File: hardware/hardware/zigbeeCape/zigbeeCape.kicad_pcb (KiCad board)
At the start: 4 copper layers, 63.5 x 54.6 mm, 144 parts, among them J1 Conn_ARM_JTAG_SWD_10, SW1 SW_MEC_5E, SW2 SW_MEC_5E, SW3 SW_MEC_5E, SW4 SW_MEC_5E, SW5 SW_MEC_5E, U1 CC1352R, U2 0.8Ghz_and_2.4GHz_Filter, U3 SMA_Antenna, U4 BeagleBone_P8, U5 BeagleBone_P9, Y1 32.768kHz, Y2 48MHz

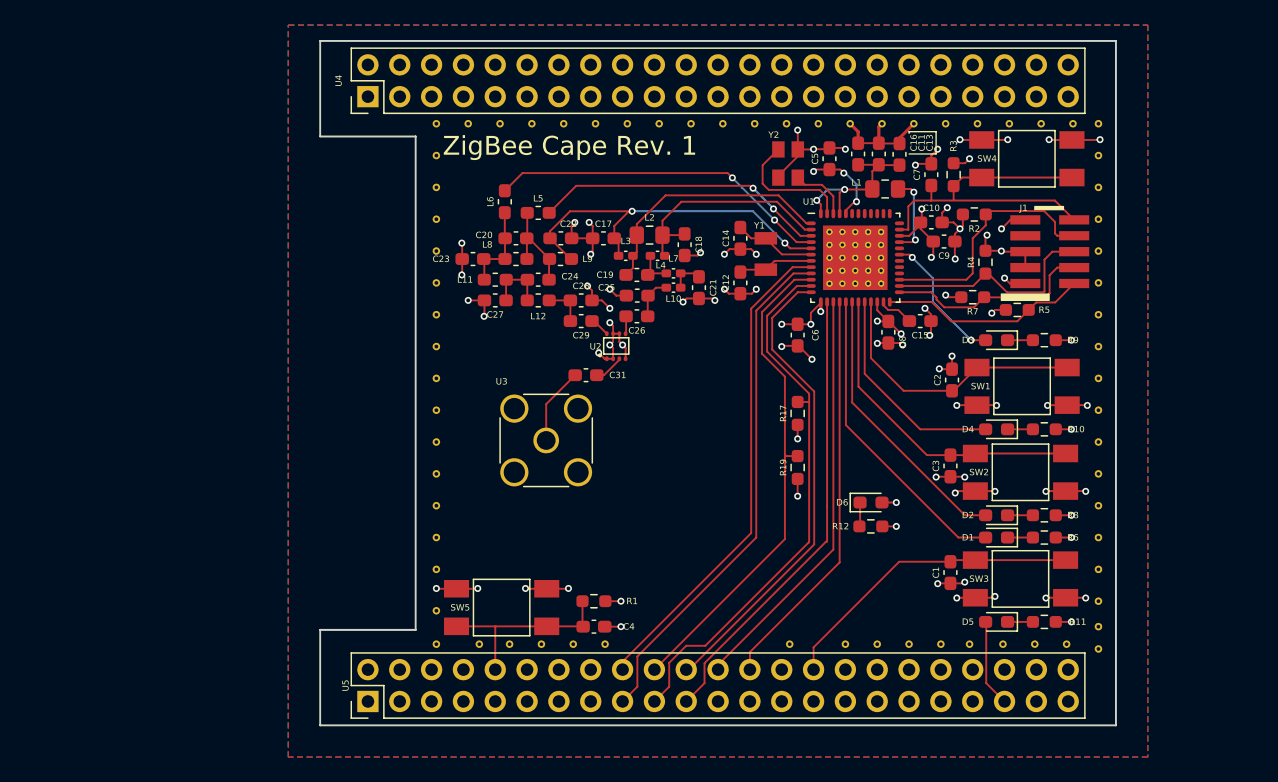
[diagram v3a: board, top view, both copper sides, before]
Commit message: Added more ground vias and silkscreen pin labels for the headers
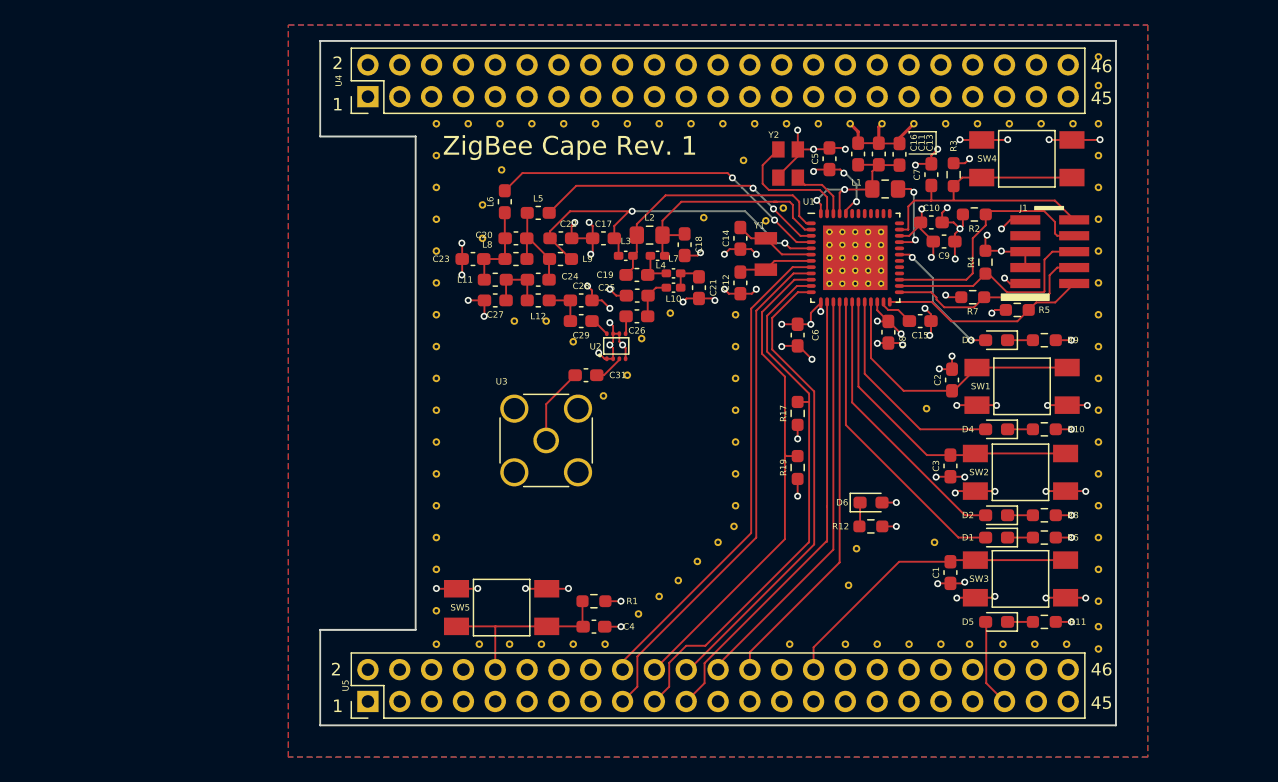
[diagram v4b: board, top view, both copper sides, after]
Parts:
- added REF**: ViaStitch-0.6mm, zigbeeCape:ViaStitch-0.6mm, F.Cu at (14.5, -44.3)
- added REF**: ViaStitch-0.6mm, zigbeeCape:ViaStitch-0.6mm, F.Cu at (25.7, -30.9)
- added REF**: ViaStitch-0.6mm, zigbeeCape:ViaStitch-0.6mm, F.Cu at (27.9, -32.9)
- added REF**: ViaStitch-0.6mm, zigbeeCape:ViaStitch-0.6mm, F.Cu at (25.4, -8.89)
- added REF**: ViaStitch-0.6mm, zigbeeCape:ViaStitch-0.6mm, F.Cu at (27.1, -10.3)
- added REF**: ViaStitch-0.6mm, zigbeeCape:ViaStitch-0.6mm, F.Cu at (28.6, -11.6)
- added REF**: ViaStitch-0.6mm, zigbeeCape:ViaStitch-0.6mm, F.Cu at (30.1, -13.1)
- added REF**: ViaStitch-0.6mm, zigbeeCape:ViaStitch-0.6mm, F.Cu at (31.8, -14.6)
- added REF**: ViaStitch-0.6mm, zigbeeCape:ViaStitch-0.6mm, F.Cu at (33.0, -15.9)
- added REF**: ViaStitch-0.6mm, zigbeeCape:ViaStitch-0.6mm, F.Cu at (33.1, -17.5)
- added REF**: ViaStitch-0.6mm, zigbeeCape:ViaStitch-0.6mm, F.Cu at (33.1, -20.1)
- added REF**: ViaStitch-0.6mm, zigbeeCape:ViaStitch-0.6mm, F.Cu at (13.0, -41.5)
- added REF**: ViaStitch-0.6mm, zigbeeCape:ViaStitch-0.6mm, F.Cu at (33.1, -22.6)
- added REF**: ViaStitch-0.6mm, zigbeeCape:ViaStitch-0.6mm, F.Cu at (33.1, -25.1)
- added REF**: ViaStitch-0.6mm, zigbeeCape:ViaStitch-0.6mm, F.Cu at (33.1, -27.7)
- added REF**: ViaStitch-0.6mm, zigbeeCape:ViaStitch-0.6mm, F.Cu at (33.1, -30.2)
- added REF**: ViaStitch-0.6mm, zigbeeCape:ViaStitch-0.6mm, F.Cu at (33.1, -32.8)
- added REF**: ViaStitch-0.6mm, zigbeeCape:ViaStitch-0.6mm, F.Cu at (62.1, -51.1)
- added REF**: ViaStitch-0.6mm, zigbeeCape:ViaStitch-0.6mm, F.Cu at (62.1, -53.3)
- added REF**: ViaStitch-0.6mm, zigbeeCape:ViaStitch-0.6mm, F.Cu at (30.6, -40.5)
- added REF**: ViaStitch-0.6mm, zigbeeCape:ViaStitch-0.6mm, F.Cu at (42.8, -14.1)
- added REF**: ViaStitch-0.6mm, zigbeeCape:ViaStitch-0.6mm, F.Cu at (42.2, -11.2)
- added REF**: ViaStitch-0.6mm, zigbeeCape:ViaStitch-0.6mm, F.Cu at (13.0, -38.9)
- added REF**: ViaStitch-0.6mm, zigbeeCape:ViaStitch-0.6mm, F.Cu at (49.0, -14.6)
- added REF**: ViaStitch-0.6mm, zigbeeCape:ViaStitch-0.6mm, F.Cu at (48.4, -25.3)
- added REF**: ViaStitch-0.6mm, zigbeeCape:ViaStitch-0.6mm, F.Cu at (35.6, -40.3)
- added REF**: ViaStitch-0.6mm, zigbeeCape:ViaStitch-0.6mm, F.Cu at (37.0, -41.3)
- added REF**: ViaStitch-0.6mm, zigbeeCape:ViaStitch-0.6mm, F.Cu at (33.8, -45.1)
- added REF**: ViaStitch-0.6mm, zigbeeCape:ViaStitch-0.6mm, F.Cu at (15.5, -32.3)
- added REF**: ViaStitch-0.6mm, zigbeeCape:ViaStitch-0.6mm, F.Cu at (18.0, -32.3)
- added REF**: ViaStitch-0.6mm, zigbeeCape:ViaStitch-0.6mm, F.Cu at (20.2, -30.6)
- added REF**: ViaStitch-0.6mm, zigbeeCape:ViaStitch-0.6mm, F.Cu at (22.6, -26.3)
- added REF**: ViaStitch-0.6mm, zigbeeCape:ViaStitch-0.6mm, F.Cu at (24.5, -27.9)
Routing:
- net /ZigBeeFiltering/2_4_GHZ_RF_N: track 18.1 -> 19.2 mm
- net /ZigBeeFiltering/2_4_GHZ_RF_P: track 20.2 -> 20.9 mm
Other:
- board text added: "1"
- board text added: "2"
- board text added: "45"
- board text added: "46"

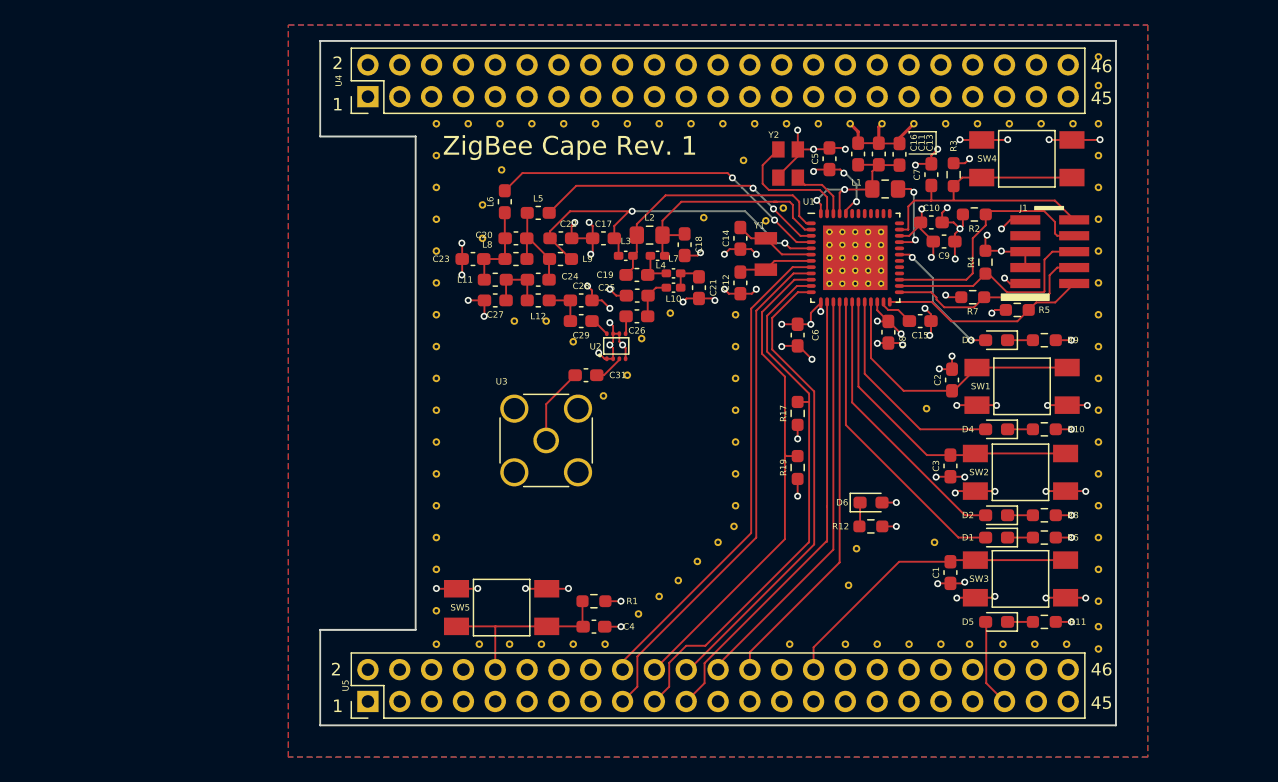
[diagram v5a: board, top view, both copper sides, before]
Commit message: Added Impedance Info and Calcuations
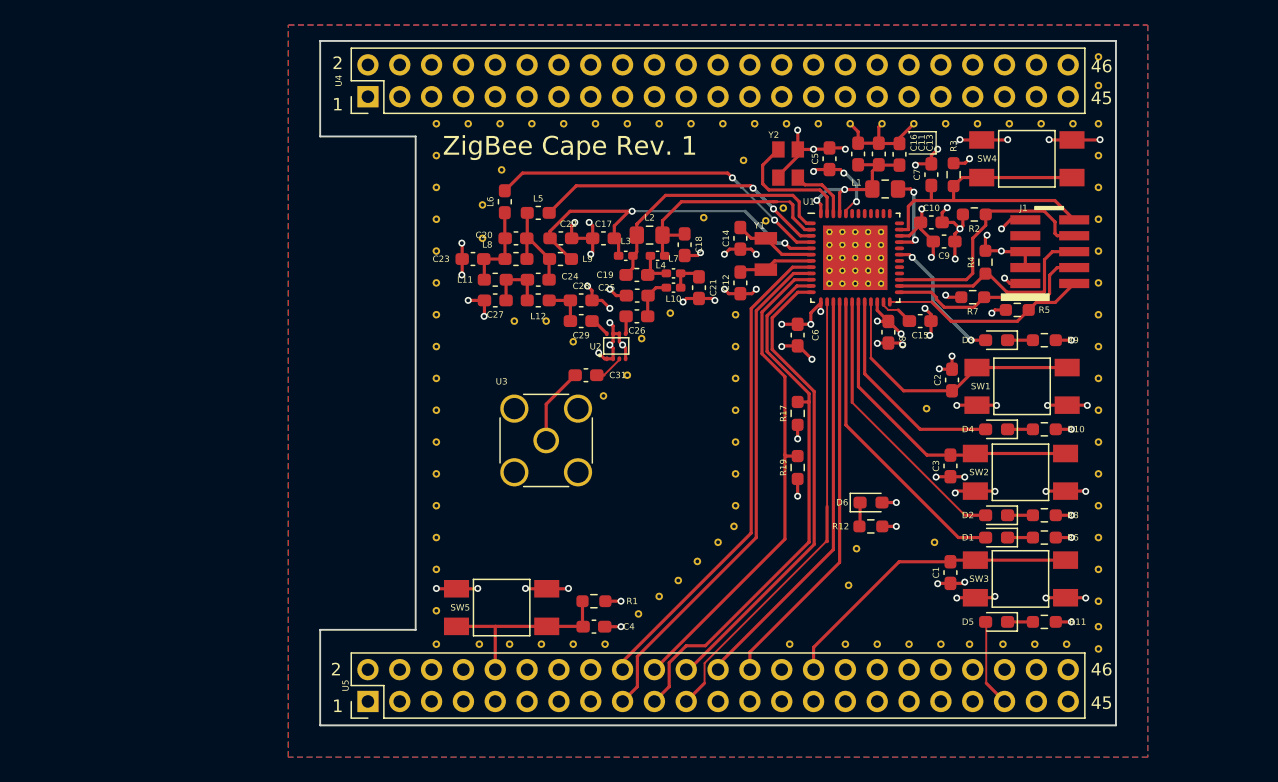
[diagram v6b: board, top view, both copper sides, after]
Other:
- net class Default: clearance 0.1524 -> 0.3175
- rule trace_clearance: 0.1524 -> 0.3175

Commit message: Rerouted main ZigBee Lines
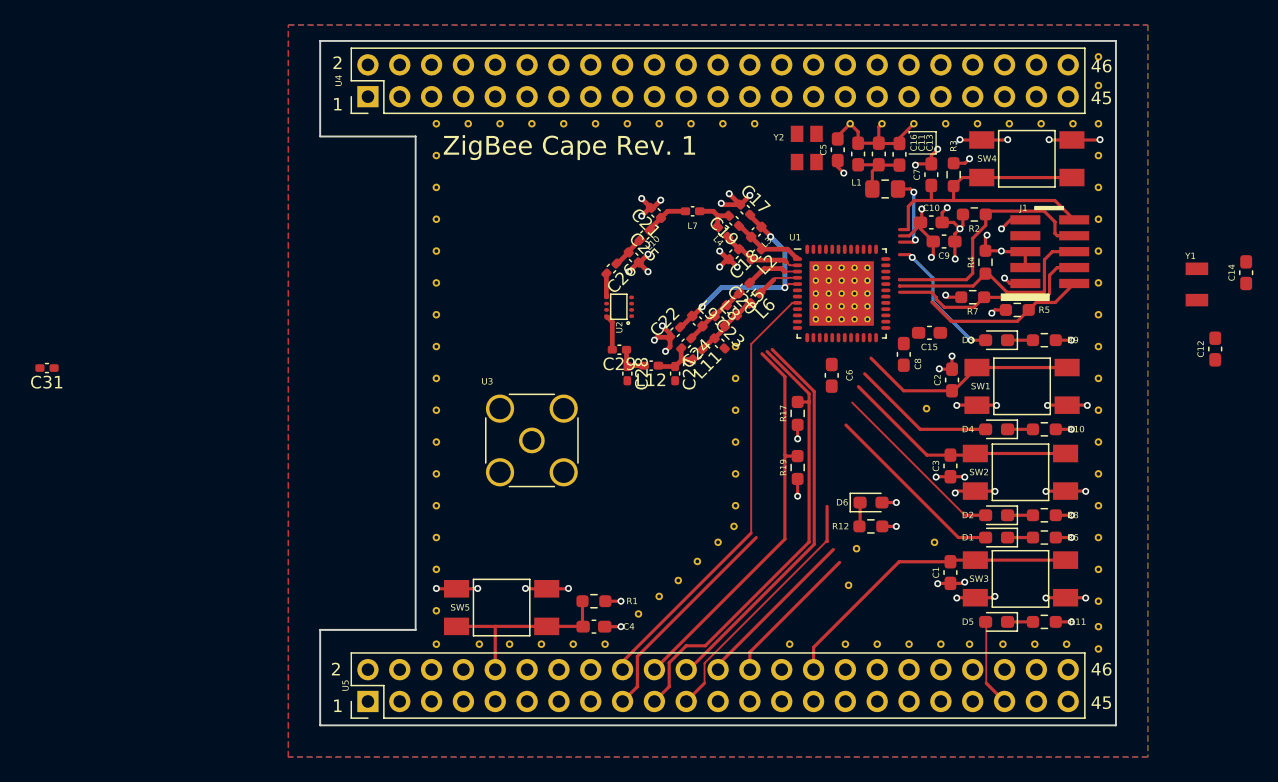
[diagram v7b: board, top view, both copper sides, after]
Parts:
- removed the REF** at (14.5, -44.3)
- removed the REF** at (25.7, -30.9)
- removed the REF** at (27.9, -32.9)
- removed the REF** at (13.0, -41.5)
- removed the REF** at (33.1, -32.8)
- removed the REF** at (30.6, -40.5)
- removed the REF** at (13.0, -38.9)
- removed the REF** at (35.6, -40.3)
- removed the REF** at (37.0, -41.3)
- removed the REF** at (33.8, -45.1)
- removed the REF** at (15.5, -32.3)
- removed the REF** at (18.0, -32.3)
- removed the REF** at (20.2, -30.6)
- removed the REF** at (22.6, -26.3)
- removed the REF** at (24.5, -27.9)
- removed the REF** at (39.8, -48.0)
- removed the REF** at (37.2, -48.0)
- C17, C18, C19, C20, C21, C22, C23, C24, C25, C26, C27, C28, C29, C31: footprint Capacitor_SMD:C_0603_1608Metric_Pad1.08x0.95mm_HandSolder -> Capacitor_SMD:C_0402_1005Metric_Pad0.74x0.62mm_HandSolder
- L11, L12, L5, L6, L8, L9: footprint Inductor_SMD:L_0603_1608Metric_Pad1.05x0.95mm_HandSolder -> Inductor_SMD:L_0402_1005Metric_Pad0.77x0.64mm_HandSolder
- L2: footprint Inductor_SMD:L_0805_2012Metric_Pad1.15x1.40mm_HandSolder -> Inductor_SMD:L_0402_1005Metric_Pad0.77x0.64mm_HandSolder
- moved C31 43.0 mm to (-21.8, -28.5)
- moved C14 40.5 mm to (73.9, -36.1)
- moved C12 38.3 mm to (71.4, -30.0)
- moved Y1 34.5 mm to (70.0, -35.4)
- moved L6 21.4 mm to (34.7, -34.1), turned to 225 degrees
- moved C23 20.8 mm to (31.9, -30.5), turned to 315 degrees
- moved C20 18.2 mm to (32.9, -33.1), turned to 315 degrees
- moved L5 17.5 mm to (33.9, -34.9), turned to 225 degrees
- moved L11 17.2 mm to (30.1, -29.6), turned to 225 degrees
- moved L8 17.0 mm to (31.9, -32.3), turned to 315 degrees
- moved C27 15.5 mm to (28.3, -28.1), turned to 270 degrees
- moved C24 12.9 mm to (29.2, -30.5), turned to 225 degrees
- moved L9 12.0 mm to (30.1, -32.3), turned to 315 degrees
- moved C22 11.8 mm to (28.3, -31.4), turned to 45 degrees
- moved C17 11.5 mm to (33.9, -41.1), turned to 315 degrees
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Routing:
- net GND: track 126.6 -> 97.3 mm, vias 73 -> 58
- net SPI_CS: track 41.2 -> 17.5 mm
- net /ZigBeeFiltering/SUB-1_GHZ_RF_N: track 27.3 -> 3.68 mm, vias 2 -> 0
- net UART_RX: track 32.3 -> 11.5 mm
- net UART_TX: track 33.2 -> 13.4 mm
- net /ZigBeeFiltering/SUB-1_GHZ_RF_P: track 23.5 -> 4.42 mm, vias 2 -> 0
- net SPI_MISO: track 36.6 -> 20.3 mm
- net /ZigBeeFiltering/2_4_GHZ_RF_P: track 20.9 -> 5.79 mm
- net +3V3: track 30.8 -> 15.9 mm, vias 16 -> 9
- net /ZigBeeFiltering/2_4_GHZ_RF_N: track 19.2 -> 6.53 mm
- net /ZigBeeFiltering/RX_TX: track 30.1 -> 17.8 mm, vias 2 -> 3
- net Net-(U1-Pad47): track 10.2 -> 0.29 mm
- net Aux_1: track 24.7 -> 14.9 mm
- net VDDR: track 14.0 -> 5.64 mm, vias 2 -> 0
- net I2C2_SDA: track 39.6 -> 31.3 mm
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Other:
- net class Default: clearance 0.3175 -> 0.254
- rule trace_clearance: 0.3175 -> 0.254
